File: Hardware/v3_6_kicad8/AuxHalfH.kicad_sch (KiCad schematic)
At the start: 26 parts, among them J23 1868076, Q25 FILL_FOOTPRINT

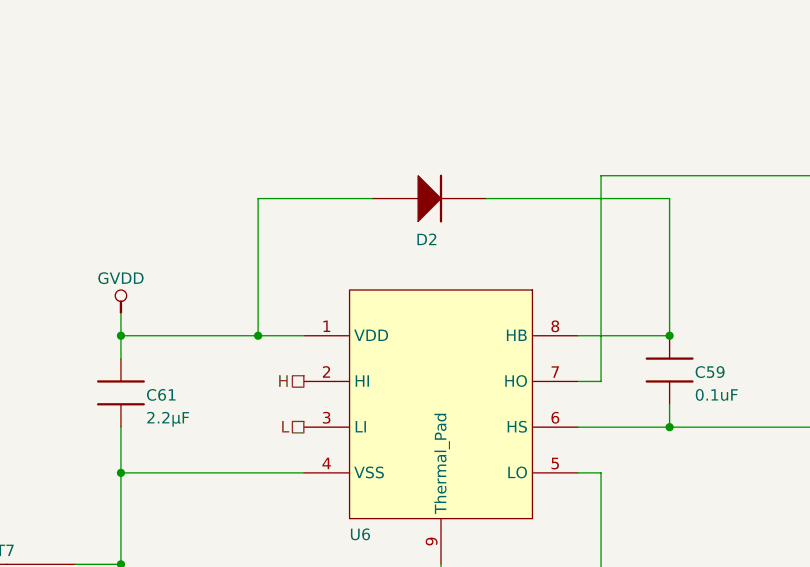
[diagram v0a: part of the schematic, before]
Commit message: modify aux schematic for gate driver value
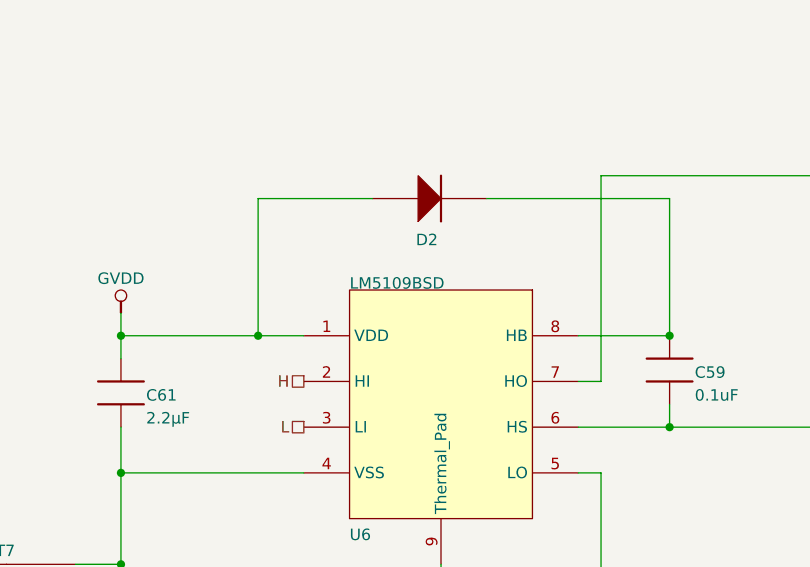
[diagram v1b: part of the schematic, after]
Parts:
- U6: value (none) -> LM5109BSD
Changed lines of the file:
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@@
 			)
 		)
-		(property "Value" ""
+		(property "Value" "LM5109BSD"
 			(at 134.62 119.2022 0)
 			(effects
@@
 				)
 				(justify left bottom)
-				(hide yes)
 			)
 		)

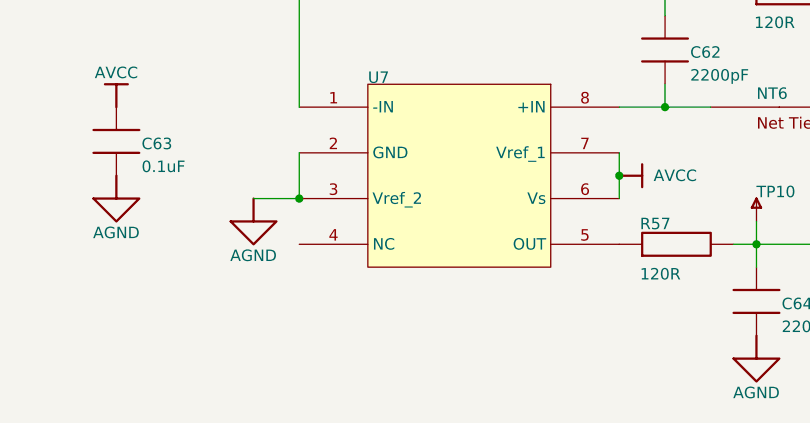
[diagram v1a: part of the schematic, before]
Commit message: assign AD8418 to current amplifier of AUX
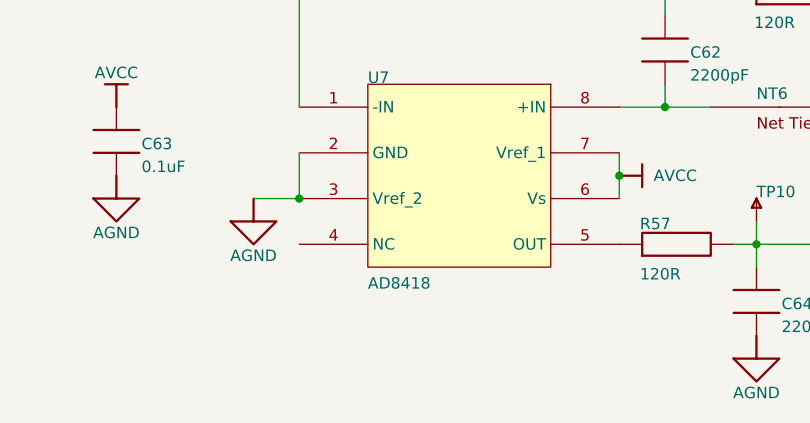
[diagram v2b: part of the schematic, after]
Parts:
- U7: value (none) -> AD8418
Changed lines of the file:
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@@
 			)
 		)
-		(property "Value" ""
+		(property "Value" "AD8418"
 			(at 185.42 218.2622 0)
 			(effects
